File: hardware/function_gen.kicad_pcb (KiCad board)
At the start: 4 copper layers, 70.5 x 60.9 mm, 81 parts, among them J11 Conn_01x08, J6 Conn_01x03_Socket, SW2 switch:SLB1470, SW3 SW_SP4T, SW4 SW_SP4T, SW5 SW_SP4T, SW6 SW_SPST, SW7 SW_SPST, U1 STM32G431CBTx, U2 AZ1117-3.3, U3 TL074

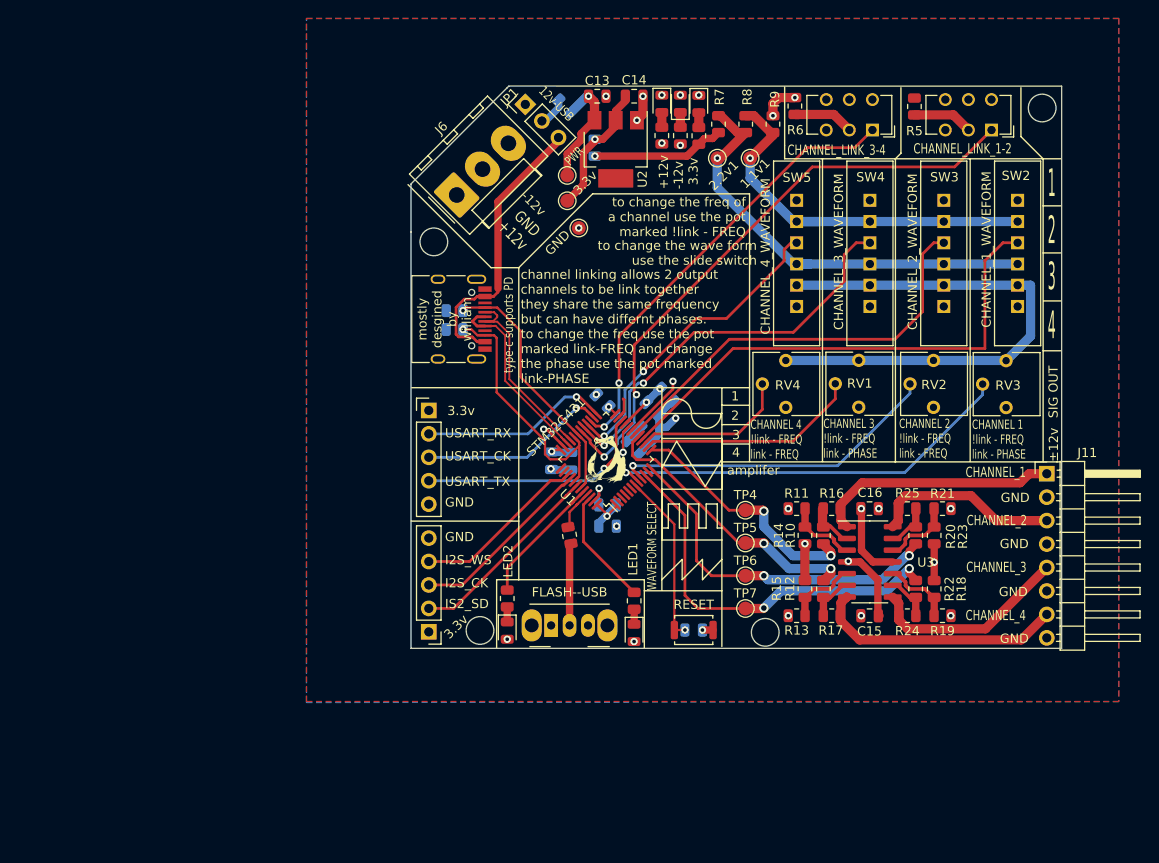
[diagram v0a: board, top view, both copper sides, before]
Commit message: updated pcb to refelect changes made in the sch
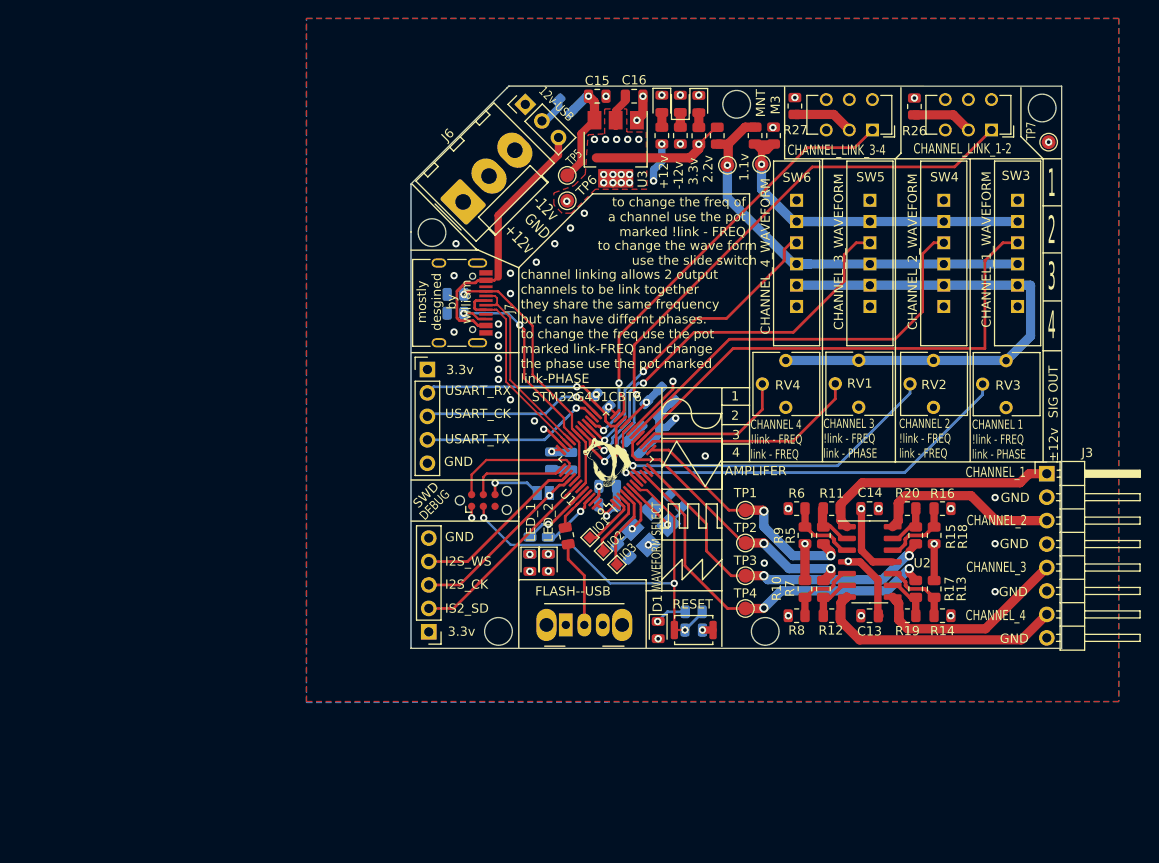
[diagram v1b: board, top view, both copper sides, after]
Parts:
- added C1: c, Capacitor_SMD:C_0805_2012Metric, B.Cu at (132.3, 101.8)
- added C4: c, Capacitor_SMD:C_0805_2012Metric, B.Cu at (138.0, 96.2)
- added D1: LED, LED_SMD:LED_0805_2012Metric, F.Cu at (136.1, 110.3)
- added J1: Conn_01x01, TestPoint:TestPoint_Pad_1.0x1.0mm, F.Cu at (130.2, 101.7)
- added J10: Conn_01x01, TestPoint:TestPoint_Pad_1.0x1.0mm, F.Cu at (128.7, 100.2)
- added J11: Conn_01x01, TestPoint:TestPoint_Pad_1.0x1.0mm, F.Cu at (131.6, 103.2)
- added J2: Conn_ARM_SWD_TagConnect_TC2030-NL, Connector:Tag-Connect_TC2030-IDC-NL_2x03_P1.27mm_Vertical, F.Cu at (117.2, 96.2)
- added SWO1: Jumper_2_Open, Jumper:SolderJumper-2_P1.3mm_Open_Pad1.0x1.5mm, B.Cu at (123.7, 95.4)
- added Y1: Crystal_GND24, Crystal:Crystal_SMD_SeikoEpson_FA238V-4Pin_3.2x2.5mm_HandSoldering, B.Cu at (135.2, 99.0)
- J7: renamed from type-c supports PD
- R2: value 0 -> 500
- R3: renamed from R30; moved to B.Cu
- R4: renamed from R32; moved to B.Cu
- moved TP7 51.7 mm to (178.4, 57.4)
- moved R2 51.4 mm to (139.9, 108.3), turned to 0 degrees
- moved D3 12.0 mm to (124.2, 103.0)
- moved R4 11.1 mm to (124.2, 101.1)
- moved D2 7.75 mm to (122.2, 103.0)
- moved R3 6.25 mm to (122.2, 101.1)
- moved J9 4.44 mm to (111.1, 82.0)
- moved C5 4.31 mm to (130.6, 94.7), turned to 180 degrees
- moved R24 1.76 mm to (114.1, 75.9)
- moved J7 1.76 mm to (113.4, 74.8)
- moved R25 1.76 mm to (114.1, 73.9)
- moved SW1 1.60 mm to (126.1, 109.7)
- moved R29 1.60 mm to (146.6, 56.7), turned to -90 degrees
- moved 1.1v1 1.41 mm to (147.3, 59.8)
- moved 2.2v1 1.33 mm to (143.6, 59.9)
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- renumbered C11 to C10, C12 to C11, C15 to C13, C16 to C14, C13 to C15, C14 to C16, C1 to C2, C2 to C3, C9 to C8, C10 to C9, D5 to D2, D6 to D3, D1 to D4, D4 to D5, D2 to D6, D3 to D7, J11 to J3, 3.3v to J8, 3.3v to J9, R15 to R10, R16 to R11, R17 to R12, R18 to R13, R19 to R14, R20 to R15, R21 to R16, R22 to R17, R23 to R18, R24 to R19, R25 to R20, R28 to R21, R26 to R22, R27 to R23, R3 to R24, R4 to R25, R5 to R26, R6 to R27, R7 to R28, R8 to R29, R9 to R30, R10 to R5, R11 to R6, R12 to R7, R13 to R8, R14 to R9, FLASH--USB to SW1, SW2 to SW3, SW3 to SW4, SW4 to SW5, SW5 to SW6, SW6 to SW7, SW7 to SW8, RESET to SW9, TP4 to TP1, TP5 to TP2, TP6 to TP3, TP7 to TP4, PWR to TP5, 3.3v to TP6, GND to TP7, U3 to U2, U2 to U3
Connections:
- net /I2S3_CK renamed /I2S3_CK-SWO
- net /OPAMP1_VINM renamed /GPIO_4
- C16 pad 1: Net-(U2-VO) -> +3.3V
- J9 pad 2: /USART3_RX -> /USART3_TX
- J9 pad 3: /USART3_CK -> /USART3_RX
- J9 pad 4: /USART3_TX -> /USART3_CK
- R2 pad 1: Net-(U2-VO) -> Net-(D1-K)
- R2 pad 2: +3.3V -> /NRST
- TP6 pad 1: Net-(U2-VO) -> +3.3V
- U1 pad 2: unconnected-(U1-PC13-Pad2) -> /GPIO_1
- U1 pad 3: unconnected-(U1-PC14-Pad3) -> /GPIO_2
- U1 pad 37: unconnected-(U1-PA13-Pad37) -> /SW_CLK
- U1 pad 38: unconnected-(U1-PA14-Pad38) -> /SW_DIO
- U1 pad 4: unconnected-(U1-PC15-Pad4) -> /GPIO_3
- U3 pad 2: Net-(U2-VO) -> +3.3V
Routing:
- net /NRST: track 19.5 -> 47.5 mm, vias 1 -> 3
- net /SW_DIO: track 0.00 -> 14.7 mm
- net Net-(U2-VO): track 14.5 -> 0.00 mm, vias 1 -> 0
- net +12V: track 107.9 -> 95.0 mm, vias 2 -> 3
- net /SW_CLK: track 0.00 -> 10.7 mm
- net /GPIO_3: track 0.00 -> 8.47 mm
- net /HSE_OUT: track 0.00 -> 8.12 mm, vias 0 -> 1
- net /HSE_IN: track 0.00 -> 7.49 mm, vias 0 -> 1
- net /GPIO_2: track 0.00 -> 6.91 mm
- net +3.3V: track 97.3 -> 104.1 mm, vias 13 -> 28
- net /debug_led2: track 13.2 -> 6.56 mm, vias 0 -> 1
- net /GPIO_1: track 0.00 -> 6.40 mm
- net Net-(J2-SWO): track 0.00 -> 6.30 mm, vias 0 -> 1
- net /debug_led1: track 14.3 -> 8.08 mm, vias 0 -> 1
- net Net-(D1-K): track 0.00 -> 3.42 mm, vias 0 -> 1
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- added copper zone on F.Cu, net +3.3V
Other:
- outline, holes or cut-outs redrawn
- board text added: "1.1v"
- board text added: "2.2v"
- board text added: "AMPLIFER"
- board text added: "DEBUG"
- board text added: "DNP"
- board text added: "FLASH--USB"
- board text added: "IO1"
- board text added: "IO2"
- board text added: "IO3"
- board text added: "JLCJLCJLCJLC"
- board text added: "LED_1"
- board text added: "LED_2"
- board text added: "M3"
- board text added: "MNT"
- board text added: "OSC_DNP use internal"
- board text added: "R1"
- board text added: "R2"
- board text added: "R3"
- board text added: "R4"
- board text added: "RESET"
- board text added: "REV2-WAITING"
- board text added: "STM32G431CBT6"
- board text added: "SWD"
- board text added: "this will only give a sig with 0 DC if VPWR is > ±12v"
- board text removed: "LED1"
- board text removed: "LED2"
- board text removed: "STM32G431"
- board text removed: "amplifer"

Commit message: tweaks power traces
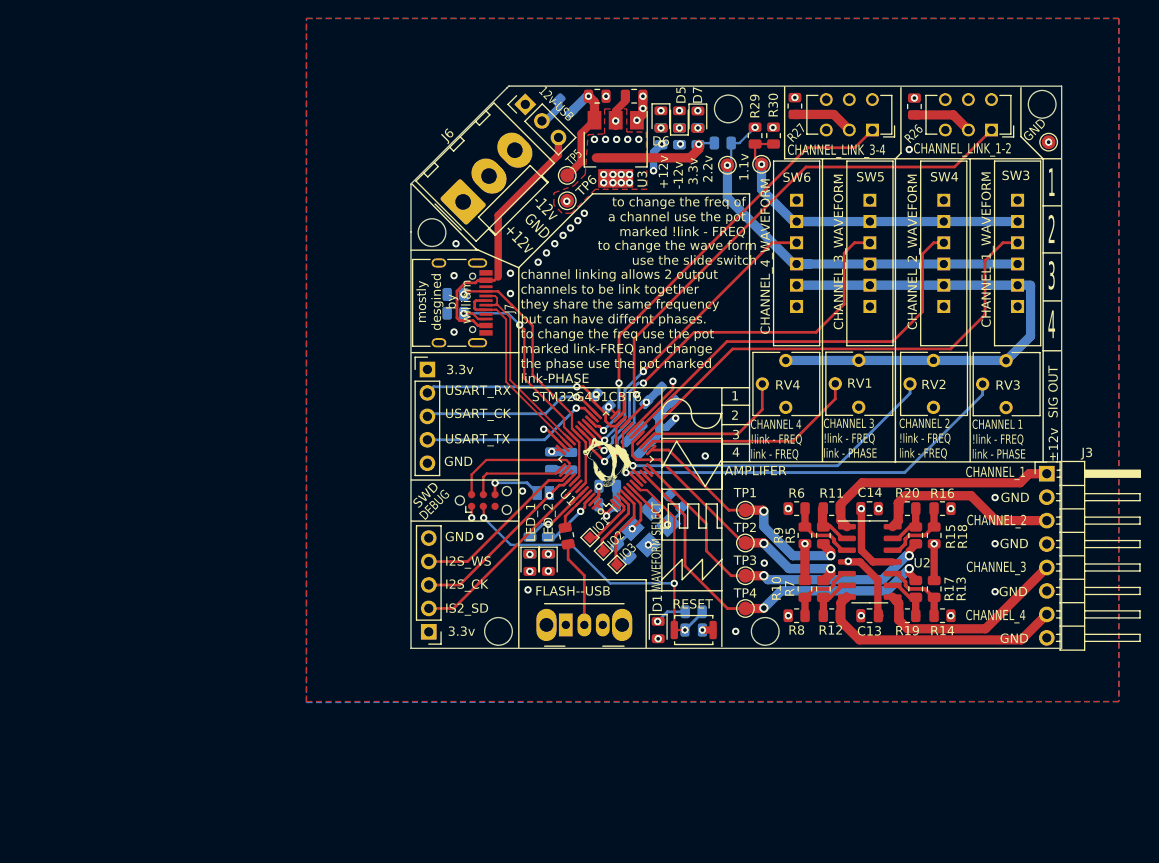
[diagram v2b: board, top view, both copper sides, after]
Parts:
- R21, R22, R23, R28: moved to B.Cu
- moved D5 1.69 mm to (138.4, 54.9)
- moved D6 1.69 mm to (136.4, 54.9)
- moved D7 1.69 mm to (140.4, 55.0)
- moved R28 1.00 mm to (143.1, 57.5), turned to 0 degrees
- moved R21 0.12 mm to (138.4, 56.8)
- moved R22 0.12 mm to (136.4, 56.8)
- moved R23 0.11 mm to (140.4, 56.8)
- renumbered TP7 to GND
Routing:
- net /ADC1_IN15: track 55.2 -> 53.0 mm
- net /USER INPUT/+1.1V: track 40.3 -> 38.7 mm
- net Net-(D6-A): track 1.59 -> 0.00 mm, vias 0 -> 1
- net Net-(D5-K): track 1.59 -> 0.00 mm, vias 0 -> 1
- net Net-(D7-A): track 1.58 -> 0.00 mm, vias 0 -> 1
- net /ADC2_IN15: track 46.3 -> 47.8 mm
- net /USER INPUT/+2.2V: track 46.5 -> 45.3 mm, vias 1 -> 2
- net +3.3V: track 104.1 -> 103.1 mm, vias 28 -> 29
- net -12V: track 78.2 -> 79.1 mm
- net /ADC1_IN5: track 35.1 -> 34.4 mm
- net GND: vias 43 -> 44
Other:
- outline, holes or cut-outs redrawn
- board text removed: "M3"
- board text removed: "MNT"

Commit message: added drawing mesurements for case desgin
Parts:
- renumbered GND to TP7
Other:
- outline, holes or cut-outs redrawn
- board text added: "135°"
- board text added: "3mm"
- board text added: "ALL MOUNTING HOLE ARE 3M SCREWS"
- board text added: "REV2-PENDING"
- board text removed: "REV2-WAITING"

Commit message: minor changes
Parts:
- moved 1.1v1 1.20 mm to (146.1, 59.9)
- moved R1 0.34 mm to (126.3, 100.4)
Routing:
- net +3.3V: track 103.1 -> 47.0 mm
- net GND: track 40.8 -> 82.9 mm, vias 44 -> 55
- net /DAC1_OUT2: track 26.7 -> 22.9 mm
- net /USART3_TX: track 28.2 -> 25.0 mm
- net /OPAMP1_VOUT: track 41.1 -> 38.7 mm
- net /FUNCTION AMPLIFIER/CH2_OUT: track 22.0 -> 20.6 mm, vias 0 -> 1
- net /USB_D-: track 22.4 -> 21.2 mm
- net /OPAMP3_VOUT: track 31.3 -> 30.6 mm
- net VBUS: track 30.4 -> 31.1 mm
- net /FUNCTION AMPLIFIER/CH3_OUT: track 27.2 -> 26.6 mm
- net -12V: track 79.1 -> 78.5 mm, vias 2 -> 3
- net +12V: track 95.1 -> 95.3 mm, vias 3 -> 4
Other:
- board size 70.5 x 60.9 mm -> 71 x 60.9 mm
- board text added: "MNT M3"
- board text added: "these needed to be well coupled"
- board text added: "this was done so there was no break in the power plane under the audio traces"
- board text removed: "135°"

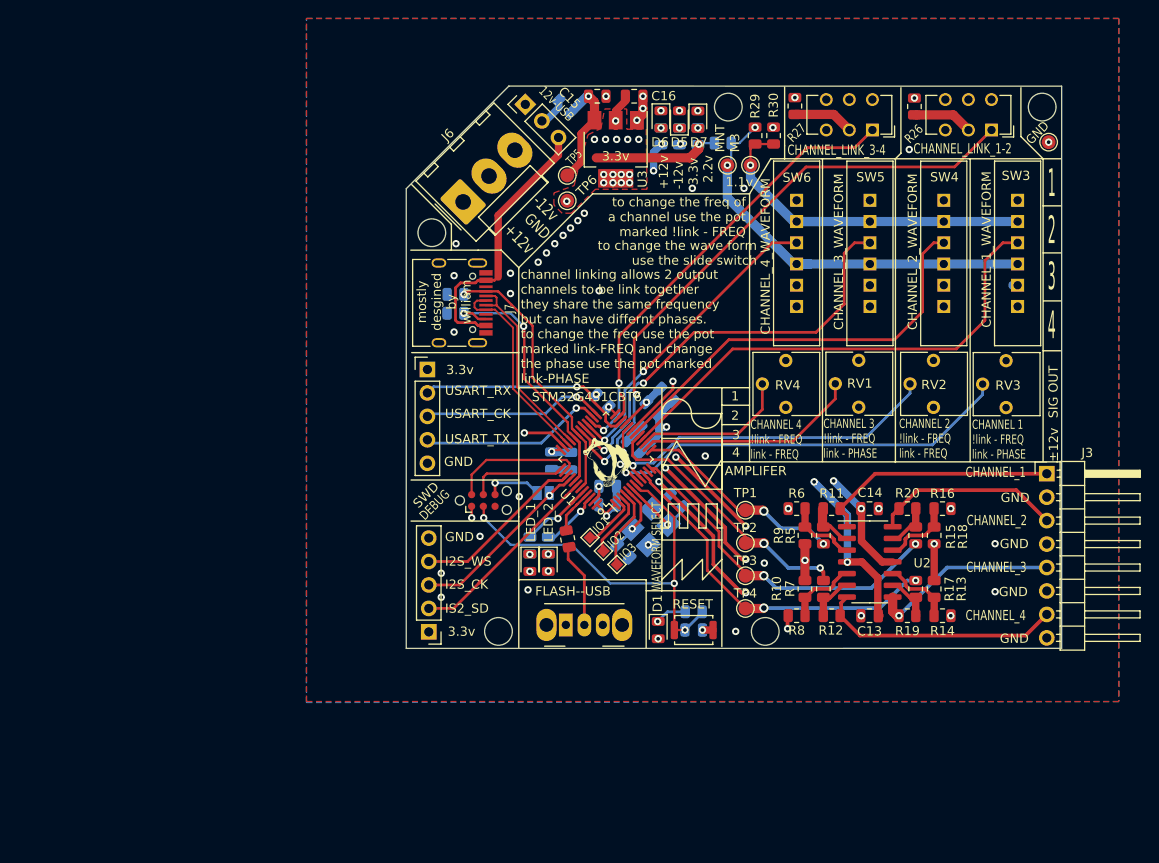
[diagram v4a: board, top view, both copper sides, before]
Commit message: updated to reflect changes made in sch
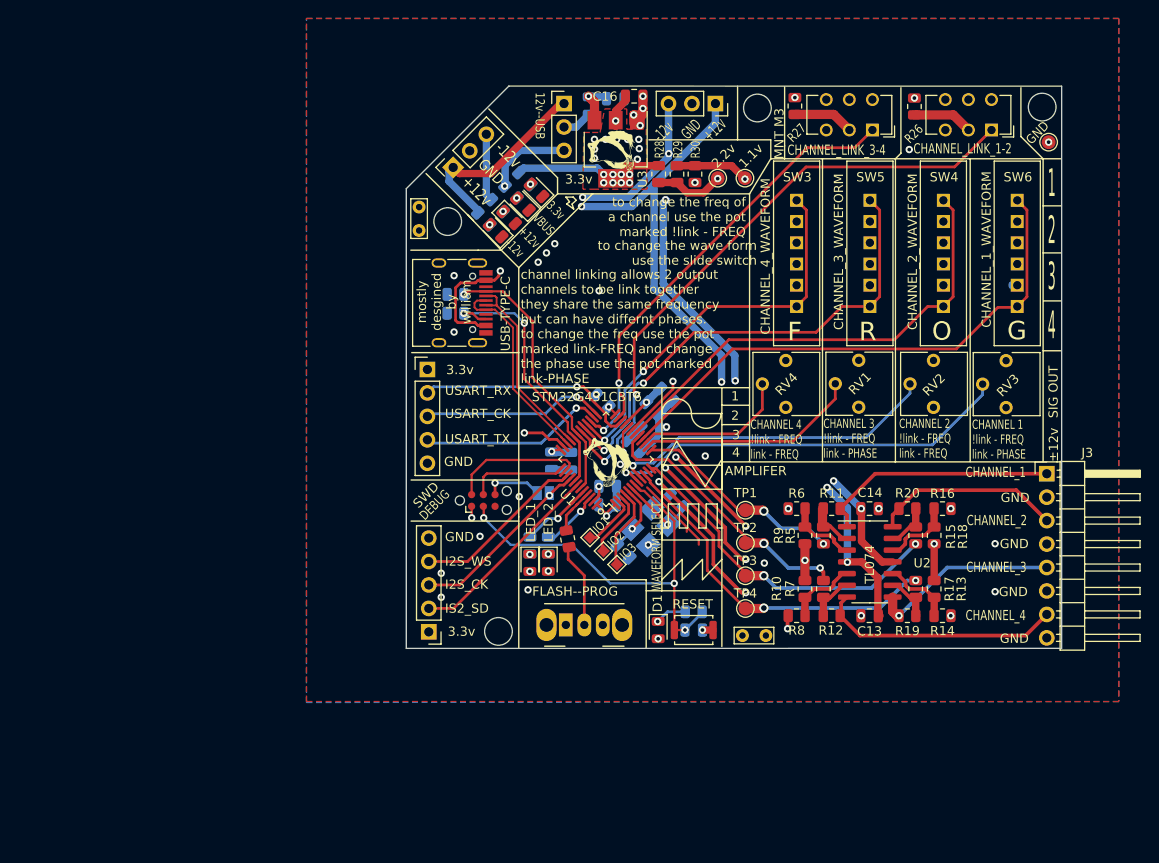
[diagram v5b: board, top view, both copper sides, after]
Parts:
- removed SW9: SW_Push, Button_Switch_SMD:SW_Push_SPST_NO_Alps_SKRK
- removed TP5: 12V/VBUS, TestPoint:TestPoint_Pad_D1.5mm
- removed TP6: 3.3V, TestPoint:TestPoint_Pad_D1.5mm
- added D8: LED, LED_SMD:LED_0805_2012Metric, F.Cu at (121.4, 64.1)
- added G***: LOGO, frogs:frog_smallest, F.Cu at (130.9, 58.5)
- added J5: Conn_01x03_Socket, Connector_PinSocket_2.54mm:PinSocket_1x03_P2.54mm_Vertical, F.Cu at (142.3, 53.2)
- added R31: 300, Resistor_SMD:R_0805_2012Metric, B.Cu at (120.2, 62.8)
- added SW2: SW_Push, Button_Switch_SMD:SW_Push_SPST_NO_Alps_SKRK, F.Cu at (139.9, 110.2)
- added TP9: GND, TestPoint:TestPoint_Bridge_Pitch2.54mm_Drill0.7mm, F.Cu at (145.2, 110.8)
- added TPGND: GND, TestPoint:TestPoint_Bridge_Pitch2.54mm_Drill0.7mm, F.Cu at (110.2, 64.4)
- C15: moved to B.Cu
- J6: footprint Connector_Molex:Molex_KK-396_A-41791-0003_1x03_P3.96mm_Vertical -> Connector_PinSocket_2.54mm:PinSocket_1x03_P2.54mm_Vertical
- R28: moved to F.Cu
- SW3: value switch:SLB1470 -> SW_SP4T
- moved SW3 23.9 mm to (151.1, 69.5)
- moved SW6 23.9 mm to (175.0, 69.5)
- moved D6 21.6 mm to (118.5, 67.0), turned to 135 degrees
- moved D5 21.3 mm to (120.0, 65.6), turned to -45 degrees
- moved R22 21.2 mm to (117.2, 65.7), turned to 135 degrees
- moved R21 21.1 mm to (118.7, 64.3), turned to 135 degrees
- moved R23 19.3 mm to (121.7, 61.4), turned to 135 degrees
- moved D7 19.1 mm to (122.9, 62.6), turned to 135 degrees
- moved R30 9.48 mm to (140.1, 60.9), turned to -90 degrees
- moved R29 9.44 mm to (138.1, 60.9), turned to 90 degrees
- moved R28 7.72 mm to (136.2, 60.9), turned to -90 degrees
- moved JP1 4.19 mm to (125.9, 53.2), turned to 0 degrees
- moved J6 3.89 mm to (113.9, 60.1), turned to 135 degrees
- moved D4 2.63 mm to (128.6, 53.4), turned to -90 degrees
- moved C15 1.97 mm to (131.4, 52.7)
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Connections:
- SW3 pad 3: /ADC1_IN15 -> /ADC1_IN5
- SW6 pad 3: /ADC1_IN5 -> /ADC1_IN15
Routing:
- net +12V: track 95.3 -> 118.8 mm
- net -12V: track 78.5 -> 93.1 mm, vias 3 -> 6
- net GND: track 82.9 -> 94.3 mm, vias 55 -> 42
- net /ADC1_IN5: track 34.4 -> 43.7 mm
- net Net-(D4-K): track 13.6 -> 5.92 mm
- net /ADC2_IN15: track 47.8 -> 54.1 mm
- net /ADC2_IN12: track 45.7 -> 51.5 mm
- net /ADC1_IN15: track 53.4 -> 59.1 mm
- net /USER INPUT/+1.1V: track 39.0 -> 41.9 mm
- net VBUS: track 31.1 -> 33.8 mm, vias 0 -> 2
- net +3.3V: track 47.0 -> 46.7 mm, vias 29 -> 31
- net /USER INPUT/+2.2V: vias 2 -> 1
- net Net-(D8-A): vias 0 -> 1
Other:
- outline, holes or cut-outs redrawn
- board text added: "12v--USB"
- board text added: "1v1"
- board text added: "2v2"
- board text added: "3v3"
- board text added: "ADC"
- board text added: "F"
- board text added: "FLASH--PROG"
- board text added: "G"
- board text added: "O"
- board text added: "R"
- board text added: "REV2-1"
- board text added: "TL074"
- board text added: "USB-TYPE-C"
- board text added: "VBUS"
- board text added: "the rat king will rise again"
- board text removed: "+12v -12v 3.3v"
- board text removed: "12v-USB"
- board text removed: "FLASH--USB"
- board text removed: "NOTES:"
- board text removed: "REV2-PENDING"

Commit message: adjusted some silk screen
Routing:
- net GND: vias 42 -> 47
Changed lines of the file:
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@@
 		(tags "resistor")
 		(property "Reference" "R30"
-			(at -2.6625 -0.062498 -90)
+			(at -2.5625 -0.062498 270)
 			(layer "F.SilkS")
 			(effects
 				(font
-					(size 1 0.7)
+					(size 1 0.6)
 					(thickness 0.15)
 				)
@@
 		(tags "resistor")
 		(property "Reference" "R28"
-			(at -2.6625 -0.1 90)
+			(at -2.5625 -0.1 90)
 			(layer "F.SilkS")
 			(effects
 				(font
-					(size 1 0.7)
+					(size 1 0.6)
 					(thickness 0.15)
 				)
@@
 		(tags "resistor")
 		(property "Reference" "R29"
-			(at 2.6625 0.112501 -90)
+			(at 2.5625 0.112501 270)
 			(layer "F.SilkS")
 			(effects
 				(font
-					(size 1 0.7)
+					(size 1 0.6)
 					(thickness 0.15)
 				)
@@
 	)
 	(gr_text "+12v"
-		(at 120.8 67.2 -45)
+		(at 119.5 68.7 315)
 		(layer "F.SilkS")
 		(effects
 			(font
-				(size 1 0.7)
+				(size 1 0.6)
 				(thickness 0.15)
 			)
@@
 		(effects
 			(font
-				(size 1 0.7)
+				(size 1 0.6)
 				(thickness 0.15)
 			)
@@
 	)
 	(gr_text "-12v"
-		(at 119.4 68.55 -45)
+		(at 120.9 67.3 315)
 		(layer "F.SilkS")
 		(effects
 			(font
-				(size 1 0.7)
+				(size 1 0.6)
 				(thickness 0.15)
 			)
@@
 	)
 	(gr_text "VBUS"
-		(at 122.35 65.8 -45)
+		(at 122.4 65.9 315)
 		(layer "F.SilkS")
 		(effects
 			(font
-				(size 1 0.7)
+				(size 1 0.6)
 				(thickness 0.15)
 			)
@@
 	)
 	(via
+		(at 144.8 76.7)
+		(size 0.8)
+		(drill 0.4)
+		(layers "F.Cu" "B.Cu")
+		(free yes)
+		(net 2)
+	)
+	(via
 		(at 140.087502 61.775)
 		(size 0.8)
@@
 	)
 	(via
+		(at 171.7 63.1)
+		(size 0.8)
+		(drill 0.4)
+		(layers "F.Cu" "B.Cu")
+		(free yes)
+		(net 2)
+	)
+	(via
 		(at 172.6 106.1)
 		(size 0.8)
@@
 	)
 	(via
+		(at 163.7 63.3)
+		(size 0.8)
+		(drill 0.4)
+		(layers "F.Cu" "B.Cu")
+		(free yes)
+		(net 2)
+	)
+	(via
 		(at 172.6 100.9)
 		(size 0.8)
@@
 		(size 0.8)
 		(drill 0.4)
+		(layers "F.Cu" "B.Cu")
+		(free yes)
+		(net 2)
+	)
+	(via
+		(at 155.7 63.3)
+		(size 0.8)
+		(drill 0.4)
+		(layers "F.Cu" "B.Cu")
+		(free yes)
+		(net 2)
+	)
+	(via
+		(at 144.4 73.4)
+		(size 0.8)
+		(drill 0.4)
